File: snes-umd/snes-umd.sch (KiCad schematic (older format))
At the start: 2 parts, among them CON101 UMD-CONN, CON102 SNES-CONN

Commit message: added ID circuit to schematic - no layout change yet
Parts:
- added C?: 0.1uF/50V, db-smt:0603, symbol C_0603
- added U?: SN74HC165PWR, db-smt:TSSOP-16, symbol SN74HC165PWR
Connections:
- net labels added: SCK, ~ID, ~MISO, ~RST
- net labels removed: ~RESET
- wire segments 94 -> 118
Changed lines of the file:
@@
 Sheet 1 1
 Title "SNES UMD Adapter"
-Date "2018-02-01"
-Rev "0.1"
+Date "2018-05-10"
+Rev "0.2"
 Comp "db Electronics"
 Comment1 "Licensed under the CERN OHL v.1.2"
@@
 	4300 2900 4875 2900
 Text Label 4825 2900 2    60   ~ 0
-~RESET
+~RST
 $Comp
 L +5V #PWR07
@@
 	7850 2950 7250 2950
 Text Label 7300 2950 0    60   ~ 0
-~RESET
+~RST
 Wire Wire Line
 	6300 5450 6150 5450
@@
 Wire Wire Line
 	7700 5450 7700 5600
-$Comp
-L UMD-CONN CON101
-U 1 1 5A7163E6
-P 6500 5550
-F 0 "CON101" H 6650 9000 60  0000 C CNN
-F 1 "UMD-CONN" H 6750 8900 60  0000 C CNN
-F 2 "db-thparts:UMD-CONN-DIP64" H 7225 9200 60  0001 C CNN
-F 3 "" H 6850 6100 60  0001 C CNN
-	1    6500 5550
-	1    0    0    -1
-$EndComp
-$Comp
-L UMD-CONN CON101
-U 2 1 5A7164A1
-P 8050 5550
-F 0 "CON101" H 8200 9000 60  0000 C CNN
-F 1 "UMD-CONN" H 8300 8900 60  0000 C CNN
-F 2 "db-thparts:UMD-CONN-DIP64" H 8775 9200 60  0001 C CNN
-F 3 "" H 8400 6100 60  0001 C CNN
-	2    8050 5550
-	1    0    0    -1
-$EndComp
 $Comp
 L SNES-CONN CON102
@@
 Wire Wire Line
 	6100 2350 6300 2350
+$Comp
+L UMD-CONN CON101
+U 1 1 5ABBC36F
+P 6500 5550
+F 0 "CON101" H 6650 9000 60  0000 C CNN
+F 1 "UMD-CONN" H 6750 8900 60  0000 C CNN
+F 2 "db-thparts:UMD-CONN-DIP64" H 7225 9200 60  0001 C CNN
+F 3 "" H 6850 6100 60  0001 C CNN
+	1    6500 5550
+	1    0    0    -1
+$EndComp
+$Comp
+L UMD-CONN CON101
+U 2 1 5ABBC462
+P 8050 5550
+F 0 "CON101" H 8200 9000 60  0000 C CNN
+F 1 "UMD-CONN" H 8300 8900 60  0000 C CNN
+F 2 "db-thparts:UMD-CONN-DIP64" H 8775 9200 60  0001 C CNN
+F 3 "" H 8400 6100 60  0001 C CNN
+	2    8050 5550
+	1    0    0    -1
+$EndComp
+$Comp
+L SN74HC165PWR U?
+U 1 1 5AF4E443
+P 3100 6500
+F 0 "U?" H 2975 6575 50  0000 C CNN
+F 1 "SN74HC165PWR" H 4000 5800 50  0000 C CNN
+F 2 "db-smt:TSSOP-16" H 3575 7200 60  0001 C CNN
+F 3 "http://www.ti.com/lit/ds/symlink/sn74hc165.pdf" H 4300 7100 60  0001 C CNN
+F 4 "296-8253-1-ND" H 3550 7000 60  0001 C CNN "Digikey"
+F 5 "IC 8-BIT SHIFT REGISTER 16-TSSOP" H 4000 6900 60  0001 C CNN "Description"
+	1    3100 6500
+	1    0    0    -1
+$EndComp
+$Comp
+L GND #PWR?
+U 1 1 5AF4E867
+P 3650 7450
+F 0 "#PWR?" H 3650 7200 50  0001 C CNN
+F 1 "GND" H 3650 7300 50  0000 C CNN
+F 2 "" H 3650 7450 50  0001 C CNN
+F 3 "" H 3650 7450 50  0001 C CNN
+	1    3650 7450
+	1    0    0    -1
+$EndComp
+Wire Wire Line
+	7850 2450 7250 2450
+Text Label 7300 2450 0    60   ~ 0
+~MISO
+Wire Wire Line
+	7850 2550 7250 2550
+Text Label 7300 2550 0    60   ~ 0
+SCK
+Wire Wire Line
+	7850 3150 7250 3150
+Text Label 7300 3150 0    60   ~ 0
+~ID
+Wire Wire Line
+	2900 6850 2300 6850
+Text Label 2350 6850 0    60   ~ 0
+~RST
+Wire Wire Line
+	4950 7050 4350 7050
+Text Label 4400 7050 0    60   ~ 0
+~MISO
+Wire Wire Line
+	2900 6950 2300 6950
+Text Label 2350 6950 0    60   ~ 0
+SCK
+Wire Wire Line
+	3650 7350 3650 7450
+$Comp
+L GND #PWR?
+U 1 1 5AF4F7F8
+P 2800 7450
+F 0 "#PWR?" H 2800 7200 50  0001 C CNN
+F 1 "GND" H 2800 7300 50  0000 C CNN
+F 2 "" H 2800 7450 50  0001 C CNN
+F 3 "" H 2800 7450 50  0001 C CNN
+	1    2800 7450
+	1    0    0    -1
+$EndComp
+Wire Wire Line
+	2900 7050 2800 7050
+Wire Wire Line
+	2800 6200 2800 7450
+Wire Wire Line
+	2900 6650 2800 6650
+Connection ~ 2800 7050
+$Comp
+L +5V #PWR?
+U 1 1 5AF4FB68
+P 4500 6150
+F 0 "#PWR?" H 4500 6000 50  0001 C CNN
+F 1 "+5V" H 4500 6290 50  0000 C CNN
+F 2 "" H 4500 6150 50  0001 C CNN
+F 3 "" H 4500 6150 50  0001 C CNN
+	1    4500 6150
+	1    0    0    -1
+$EndComp
+$Comp
+L C_0603 C?
+U 1 1 5AF50199
+P 4800 6650
+F 0 "C?" V 4550 6600 50  0000 L CNN
+F 1 "0.1uF/50V" V 4650 6600 50  0000 L CNN
+F 2 "db-smt:0603" H 5300 6550 30  0001 C CNN
+F 3 "" H 4825 6750 60  0001 C CNN
+F 4 "445-5666-1-ND" H 5225 6625 60  0001 C CNN "Digikey"
+F 5 "CAP CER 0.1UF 50V X7R 0603" H 5225 6725 60  0001 C CNN "Description"
+	1    4800 6650
+	0    1    1    0
+$EndComp
+$Comp
+L GND #PWR?
+U 1 1 5AF50358
+P 5050 6750
+F 0 "#PWR?" H 5050 6500 50  0001 C CNN
+F 1 "GND" H 5050 6600 50  0000 C CNN
+F 2 "" H 5050 6750 50  0001 C CNN
+F 3 "" H 5050 6750 50  0001 C CNN
+	1    5050 6750
+	1    0    0    -1
+$EndComp
+Wire Wire Line
+	4350 6650 4650 6650
+Wire Wire Line
+	4500 6150 4500 6650
+Connection ~ 4500 6650
+Wire Wire Line
+	4950 6650 5050 6650
+Wire Wire Line
+	5050 6650 5050 6750
+Wire Wire Line
+	3900 6300 3900 6200
+Wire Wire Line
+	3900 6200 4500 6200
+Connection ~ 4500 6200
+Wire Wire Line
+	4000 6300 4000 6200
+Connection ~ 4000 6200
+Wire Wire Line
+	3800 6300 3800 6200
+Wire Wire Line
+	3800 6200 2800 6200
+Connection ~ 2800 6650
+Wire Wire Line
+	3300 6300 3300 6200
+Connection ~ 3300 6200
+Wire Wire Line
+	3400 6300 3400 6200
+Connection ~ 3400 6200
+Wire Wire Line
+	3500 6300 3500 6200
+Connection ~ 3500 6200
+Wire Wire Line
+	3600 6300 3600 6200
+Connection ~ 3600 6200
+Wire Wire Line
+	3700 6300 3700 6200
+Connection ~ 3700 6200
 $EndSCHEMATC

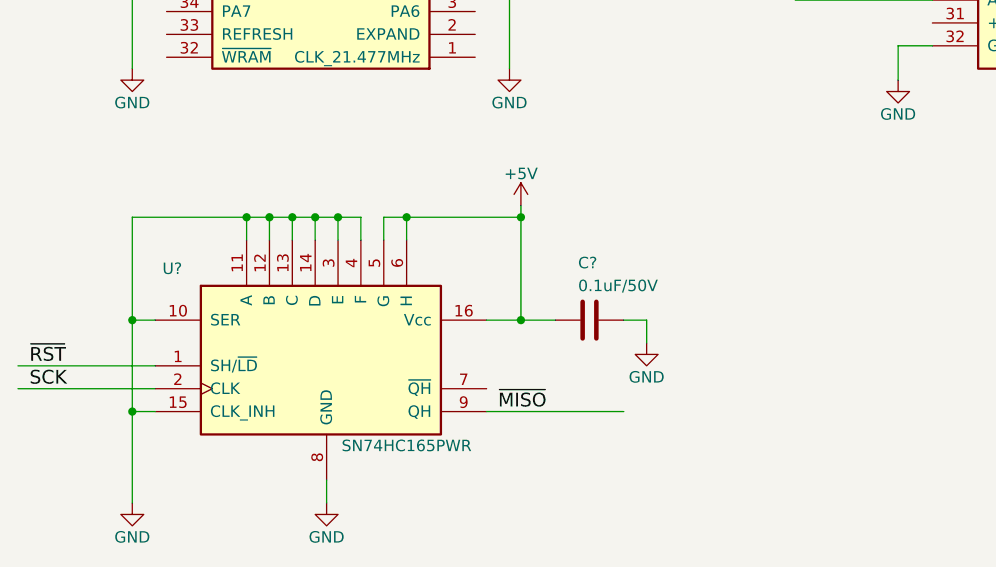
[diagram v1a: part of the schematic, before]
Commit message: adding ID register to schematic
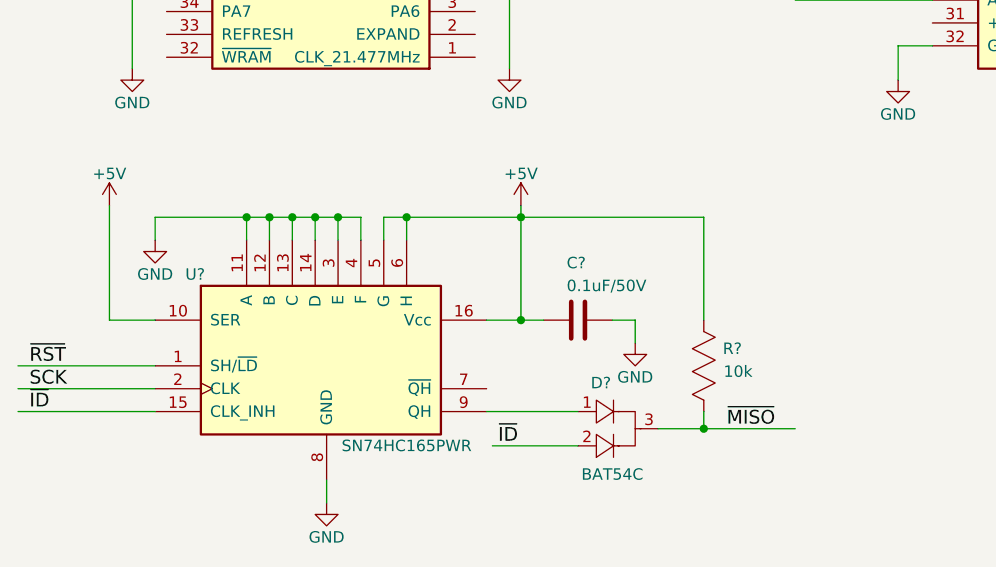
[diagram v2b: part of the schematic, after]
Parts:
- added D?: BAT54C, db-smt:SOT23, symbol BAT54C
- added R?: 10k, db-smt:0603, symbol R_0603
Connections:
- wire segments 118 -> 123
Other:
- moved on the sheet: C?
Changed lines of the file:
@@
 U 1 1 5AF4E443
 P 3100 6500
-F 0 "U?" H 2975 6575 50  0000 C CNN
+F 0 "U?" H 3075 6550 50  0000 C CNN
 F 1 "SN74HC165PWR" H 4000 5800 50  0000 C CNN
 F 2 "db-smt:TSSOP-16" H 3575 7200 60  0001 C CNN
@@
 Text Label 2350 6850 0    60   ~ 0
 ~RST
-Wire Wire Line
-	4950 7050 4350 7050
-Text Label 4400 7050 0    60   ~ 0
+Text Label 5400 7125 0    60   ~ 0
 ~MISO
 Wire Wire Line
@@
 L GND #PWR?
 U 1 1 5AF4F7F8
-P 2800 7450
-F 0 "#PWR?" H 2800 7200 50  0001 C CNN
-F 1 "GND" H 2800 7300 50  0000 C CNN
-F 2 "" H 2800 7450 50  0001 C CNN
-F 3 "" H 2800 7450 50  0001 C CNN
-	1    2800 7450
+P 2900 6300
+F 0 "#PWR?" H 2900 6050 50  0001 C CNN
+F 1 "GND" H 2900 6150 50  0000 C CNN
+F 2 "" H 2900 6300 50  0001 C CNN
+F 3 "" H 2900 6300 50  0001 C CNN
+	1    2900 6300
 	1    0    0    -1
 $EndComp
-Wire Wire Line
-	2900 7050 2800 7050
-Wire Wire Line
-	2800 6200 2800 7450
-Wire Wire Line
-	2900 6650 2800 6650
-Connection ~ 2800 7050
 $Comp
 L +5V #PWR?
@@
 L C_0603 C?
 U 1 1 5AF50199
-P 4800 6650
-F 0 "C?" V 4550 6600 50  0000 L CNN
-F 1 "0.1uF/50V" V 4650 6600 50  0000 L CNN
-F 2 "db-smt:0603" H 5300 6550 30  0001 C CNN
-F 3 "" H 4825 6750 60  0001 C CNN
-F 4 "445-5666-1-ND" H 5225 6625 60  0001 C CNN "Digikey"
-F 5 "CAP CER 0.1UF 50V X7R 0603" H 5225 6725 60  0001 C CNN "Description"
-	1    4800 6650
+P 4750 6650
+F 0 "C?" V 4500 6600 50  0000 L CNN
+F 1 "0.1uF/50V" V 4600 6600 50  0000 L CNN
+F 2 "db-smt:0603" H 5250 6550 30  0001 C CNN
+F 3 "" H 4775 6750 60  0001 C CNN
+F 4 "445-5666-1-ND" H 5175 6625 60  0001 C CNN "Digikey"
+F 5 "CAP CER 0.1UF 50V X7R 0603" H 5175 6725 60  0001 C CNN "Description"
+	1    4750 6650
 	0    1    1    0
 $EndComp
@@
 L GND #PWR?
 U 1 1 5AF50358
-P 5050 6750
-F 0 "#PWR?" H 5050 6500 50  0001 C CNN
-F 1 "GND" H 5050 6600 50  0000 C CNN
-F 2 "" H 5050 6750 50  0001 C CNN
-F 3 "" H 5050 6750 50  0001 C CNN
-	1    5050 6750
+P 5000 6750
+F 0 "#PWR?" H 5000 6500 50  0001 C CNN
+F 1 "GND" H 5000 6600 50  0000 C CNN
+F 2 "" H 5000 6750 50  0001 C CNN
+F 3 "" H 5000 6750 50  0001 C CNN
+	1    5000 6750
 	1    0    0    -1
 $EndComp
 Wire Wire Line
-	4350 6650 4650 6650
+	4900 6650 5000 6650
 Wire Wire Line
-	4500 6150 4500 6650
-Connection ~ 4500 6650
-Wire Wire Line
-	4950 6650 5050 6650
-Wire Wire Line
-	5050 6650 5050 6750
+	5000 6650 5000 6750
 Wire Wire Line
 	3900 6300 3900 6200
-Wire Wire Line
-	3900 6200 4500 6200
 Connection ~ 4500 6200
 Wire Wire Line
@@
 Connection ~ 4000 6200
 Wire Wire Line
-	3800 6300 3800 6200
+	3800 6200 3800 6300
 Wire Wire Line
-	3800 6200 2800 6200
-Connection ~ 2800 6650
+	2900 6200 3800 6200
 Wire Wire Line
 	3300 6300 3300 6200
@@
 	3700 6300 3700 6200
 Connection ~ 3700 6200
+Wire Wire Line
+	2900 7050 2300 7050
+Text Label 2350 7050 0    60   ~ 0
+~ID
+Wire Wire Line
+	2900 6200 2900 6300
+$Comp
+L +5V #PWR?
+U 1 1 5AF5D4F4
+P 2700 6150
+F 0 "#PWR?" H 2700 6000 50  0001 C CNN
+F 1 "+5V" H 2700 6290 50  0000 C CNN
+F 2 "" H 2700 6150 50  0001 C CNN
+F 3 "" H 2700 6150 50  0001 C CNN
+	1    2700 6150
+	1    0    0    -1
+$EndComp
+Wire Wire Line
+	2700 6150 2700 6650
+Wire Wire Line
+	2700 6650 2900 6650
+Wire Wire Line
+	4500 6150 4500 6650
+Wire Wire Line
+	4350 6650 4600 6650
+$Comp
+L BAT54C D?
+U 1 1 5AF5E292
+P 4825 7050
+F 0 "D?" H 4850 7175 50  0000 C CNN
+F 1 "BAT54C" H 4900 6775 50  0000 C CNN
+F 2 "db-smt:SOT23" H 5125 7375 60  0001 C CNN
+F 3 "https://www.fairchildsemi.com/datasheets/BA/BAT54.pdf" H 6125 7550 60  0001 C CNN
+F 4 "BAT54CFSCT-ND" H 5175 7450 60  0001 C CNN "Digikey"
+F 5 "DIODE ARRAY SCHOTTKY 30V SOT23-3" H 5675 7275 60  0001 C CNN "Description"
+	1    4825 7050
+	1    0    0    -1
+$EndComp
+Wire Wire Line
+	4750 7050 4350 7050
+Wire Wire Line
+	4750 7200 4375 7200
+Text Label 4400 7200 0    60   ~ 0
+~ID
+Wire Wire Line
+	3900 6200 5300 6200
+Connection ~ 4500 6650
+$Comp
+L R_0603 R?
+U 1 1 5AF5E5E3
+P 5300 6850
+F 0 "R?" H 5425 6925 50  0000 C CNN
+F 1 "10k" H 5450 6825 50  0000 C CNN
+F 2 "db-smt:0603" H 5600 6750 30  0001 C CNN
+F 3 "" H 5400 6850 30  0001 C CNN
+F 4 "#ND" H 5550 6825 60  0001 C CNN "Digikey"
+F 5 "#ND" H 5550 6925 60  0001 C CNN "Description"
+	1    5300 6850
+	1    0    0    -1
+$EndComp
+Wire Wire Line
+	5300 6200 5300 6650
+Wire Wire Line
+	5100 7125 5700 7125
+Wire Wire Line
+	5300 7125 5300 7050
+Connection ~ 5300 7125
 $EndSCHEMATC

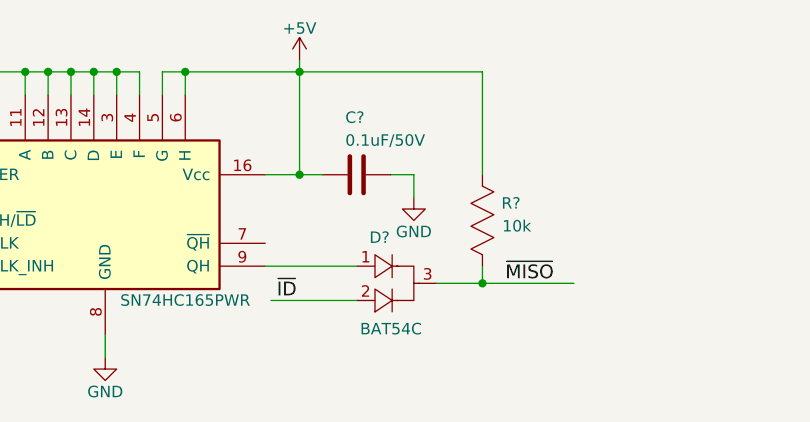
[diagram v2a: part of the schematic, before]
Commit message: changed BAT54A to BAT54S
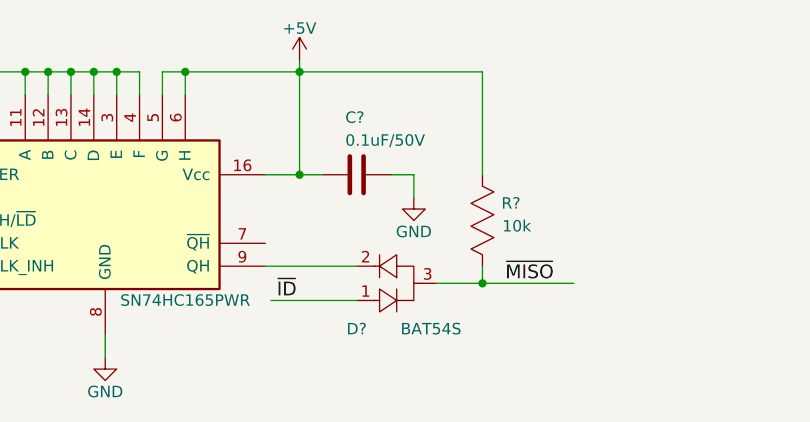
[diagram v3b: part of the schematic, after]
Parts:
- removed D?: BAT54C, db-smt:SOT23, symbol BAT54C
- added D?: BAT54S, db-smt:SOT23, symbol BAT54S
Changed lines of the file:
@@
 Sheet 1 1
 Title "SNES UMD Adapter"
-Date "2018-05-10"
+Date "2018-08-10"
 Rev "0.2"
 Comp "db Electronics"
@@
 55 70 33 82 AD 8D 87 68 2D 82 9A 22 84 9A D5 6D AC 9D 3F 96 26 7E 21 1F FE 4D 60 29 EC 04 00 00
 00 E8 29 58 2C 03 00 00 C0 A8 FD 1F 1F 82 A8 A4 9D 50 0C 54 00 00 00 00 49 45 4E 44 AE 42 60 82
+F0
 EndData
 $EndBitmap
@@
 Wire Wire Line
 	4350 6650 4600 6650
-$Comp
-L BAT54C D?
-U 1 1 5AF5E292
-P 4825 7050
-F 0 "D?" H 4850 7175 50  0000 C CNN
-F 1 "BAT54C" H 4900 6775 50  0000 C CNN
-F 2 "db-smt:SOT23" H 5125 7375 60  0001 C CNN
-F 3 "https://www.fairchildsemi.com/datasheets/BA/BAT54.pdf" H 6125 7550 60  0001 C CNN
-F 4 "BAT54CFSCT-ND" H 5175 7450 60  0001 C CNN "Digikey"
-F 5 "DIODE ARRAY SCHOTTKY 30V SOT23-3" H 5675 7275 60  0001 C CNN "Description"
-	1    4825 7050
-	1    0    0    -1
-$EndComp
 Wire Wire Line
 	4750 7050 4350 7050
@@
 	5300 7125 5300 7050
 Connection ~ 5300 7125
+$Comp
+L BAT54S D?
+U 1 1 5B6DC490
+P 4825 7200
+F 0 "D?" H 4750 7325 50  0000 C CNN
+F 1 "BAT54S" H 5075 7325 50  0000 C CNN
+F 2 "db-smt:SOT23" H 5125 7525 60  0001 C CNN
+F 3 "https://www.fairchildsemi.com/datasheets/BA/BAT54.pdf" H 6125 7700 60  0001 C CNN
+F 4 "BAT54SFSCT-ND" H 5175 7600 60  0001 C CNN "Digikey"
+F 5 "DIODE ARRAY SCHOTTKY 30V SOT23-3" H 5675 7425 60  0001 C CNN "Description"
+	1    4825 7200
+	1    0    0    1
+$EndComp
 $EndSCHEMATC
